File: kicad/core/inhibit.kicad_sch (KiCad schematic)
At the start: 7 parts, among them J5 INH_EN_n, Q4 FDS8958A, Q7 2N7002, U7 TC4427A, U8 TC4427A

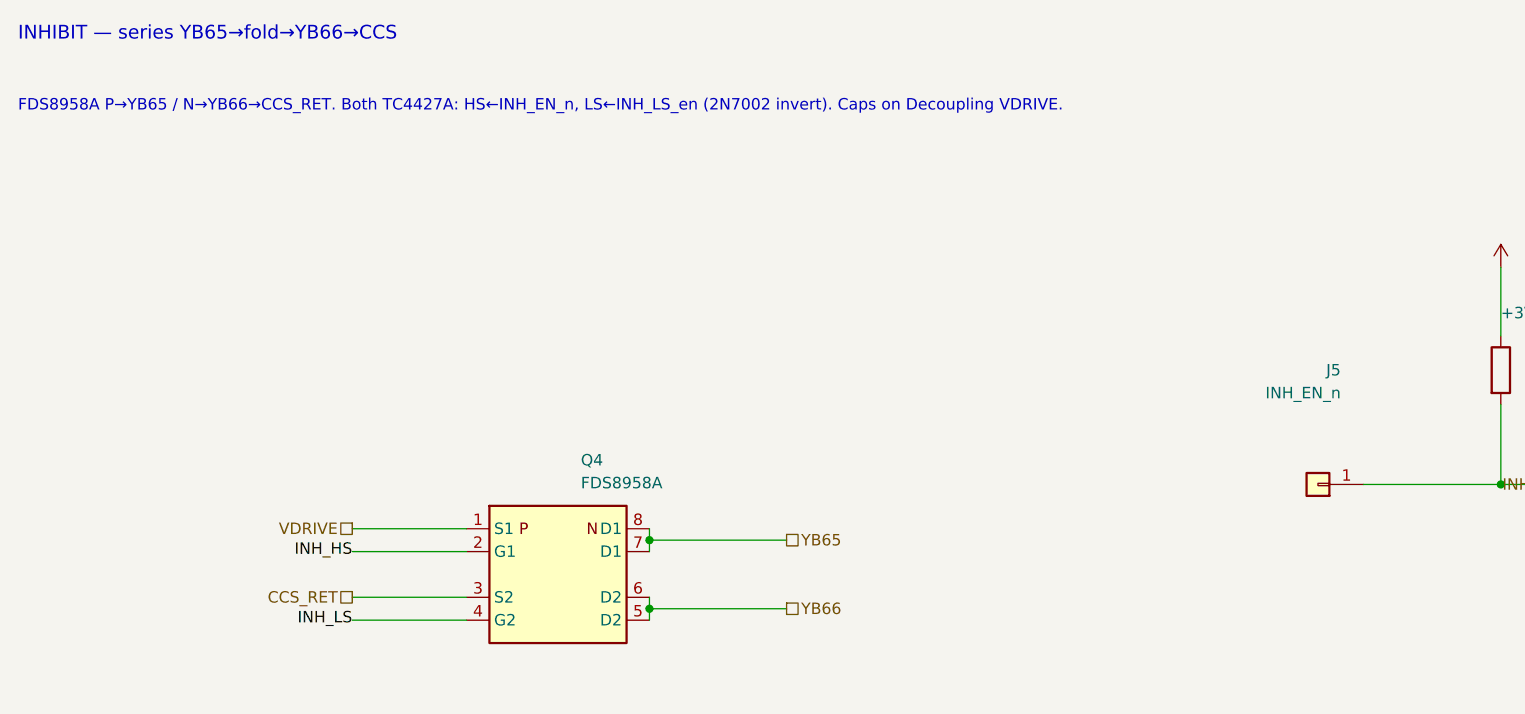
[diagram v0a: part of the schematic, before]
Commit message: Docs updated to match physical core layout.
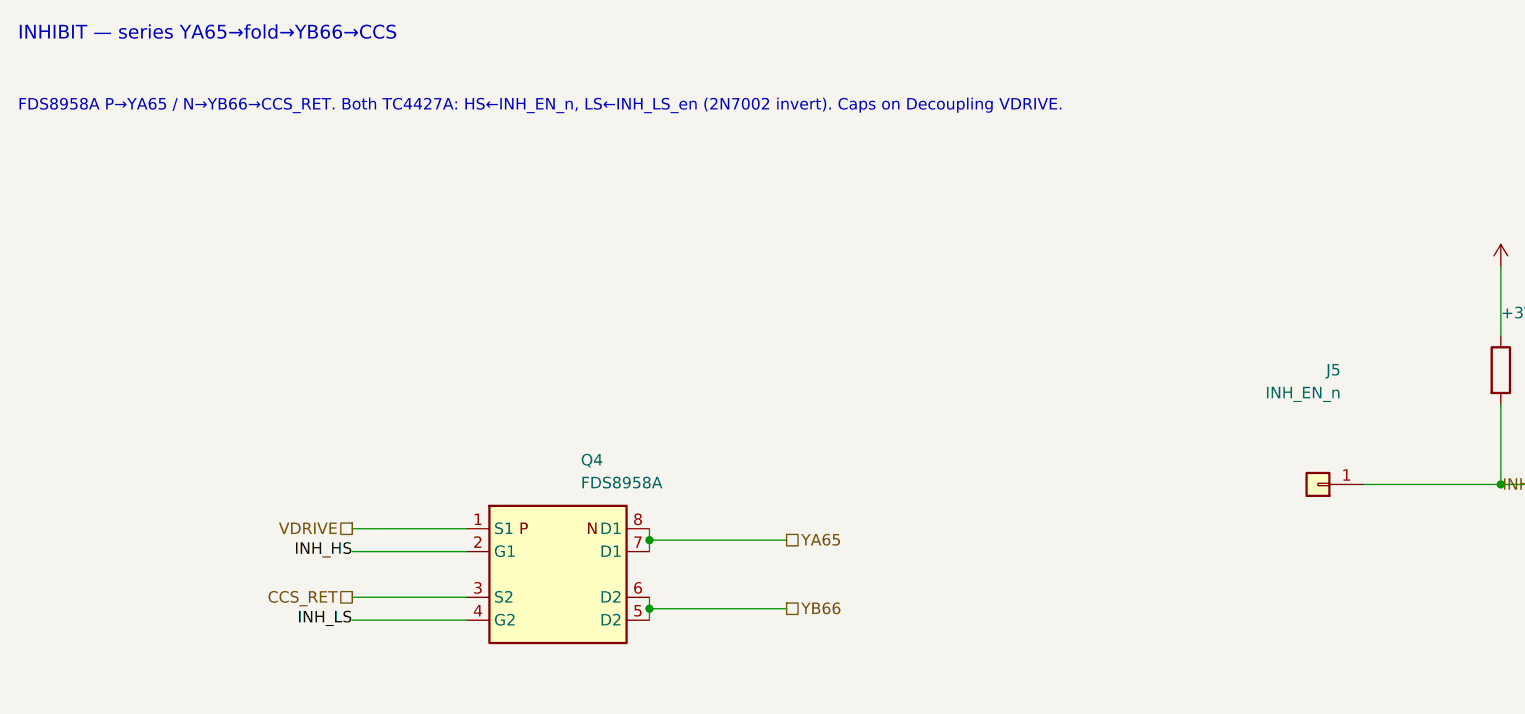
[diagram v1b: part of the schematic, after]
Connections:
- net YB65 renamed YA65
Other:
- note added: "FDS8958A P→YA65 / N→YB66→CCS_RET. Both TC4427A: HS←INH_EN_n, LS←INH_LS_en (2N7002 invert). Caps on Decoupling VDRIVE."
- note added: "INHIBIT — series YA65→fold→YB66→CCS"
- note removed: "FDS8958A P→YB65 / N→YB66→CCS_RET. Both TC4427A: HS←INH_EN_n, LS←INH_LS_en (2N7002 invert). Caps on Decoupling VDRIVE."
- note removed: "INHIBIT — series YB65→fold→YB66→CCS"
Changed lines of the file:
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@@
 	(title_block
 		(title "Inhibit")
-		(comment 1 "Series inhibit on folded sense; TC4427A×2")
-	)
-	(text "INHIBIT — series YB65→fold→YB66→CCS"
+		(comment 1 "Series inhibit YA65 through center tap to YB66; TC4427A×2")
+	)
+	(text "INHIBIT — series YA65→fold→YB66→CCS"
 		(exclude_from_sim no)
 		(at 20 20 0)
@@
 		)
 	)
-	(text "FDS8958A P→YB65 / N→YB66→CCS_RET. Both TC4427A: HS←INH_EN_n, LS←INH_LS_en (2N7002 invert). Caps on Decoupling VDRIVE."
+	(text "FDS8958A P→YA65 / N→YB66→CCS_RET. Both TC4427A: HS←INH_EN_n, LS←INH_LS_en (2N7002 invert). Caps on Decoupling VDRIVE."
 		(exclude_from_sim no)
 		(at 20 28 0)
@@
 		)
 	)
-	(hierarchical_label "YB65"
+	(hierarchical_label "YA65"
 		(shape passive)
 		(at 105.4 76.19 0)
